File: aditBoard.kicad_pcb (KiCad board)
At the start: 4 copper layers, 36 parts, among them J1 USB_C_Receptacle_USB2.0, J2 Hashboard0, U2 W25X40CLUXIG TR, U3 RP2040, U4 RT9080-33GJ5, Y1 12MHz

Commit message: pretty much routed
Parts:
- removed R24, R26, R28: 4.7K, Resistor_SMD:R_0805_2012Metric
- added R1: 10k, Resistor_SMD:R_0402_1005Metric, F.Cu at (122.0, 97.8)
- J2: footprint Connector_PinHeader_2.00mm:PinHeader_2x09_P2.00mm_Horizontal -> aditBoard:PinHeader_2x09_P2.00mm_Horizontal
- R25, R27, R29: footprint Resistor_SMD:R_0805_2012Metric -> Resistor_SMD:R_0402_1005Metric
- TP1, TP4, TP5, TP6: moved to B.Cu
- moved C17 35.6 mm to (115.1, 99.2), turned to 90 degrees
- moved R4 35.0 mm to (115.1, 101.3), turned to -90 degrees
- moved J1 32.9 mm to (121.0, 107.1), turned to 0 degrees
- moved C18 32.9 mm to (116.9, 97.2)
- moved C11 32.7 mm to (115.0, 94.5), turned to 90 degrees
- moved C14 31.7 mm to (115.1, 84.2), turned to -90 degrees
- moved C13 30.7 mm to (116.0, 94.5), turned to 90 degrees
- moved R3 30.1 mm to (120.0, 98.9), turned to 90 degrees
- moved C9 29.6 mm to (115.1, 97.4), turned to -90 degrees
- moved R2 29.6 mm to (120.9, 98.9), turned to 90 degrees
- moved C8 29.4 mm to (115.5, 96.0)
- moved C16 29.3 mm to (123.6, 100.9), turned to 90 degrees
- moved C15 29.2 mm to (123.1, 97.8), turned to -90 degrees
- moved C10 27.9 mm to (116.2, 84.2), turned to -90 degrees
- moved C7 27.8 mm to (115.6, 81.6)
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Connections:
- net /A00 renamed /A0
- net /A10 renamed /A1
- net /A20 renamed /A2
- J2 pad 11: /TXD0 -> /TXD
- J2 pad 12: /RXD0 -> /RXD
- J2 pad 15: /RST0 -> /RST
- J2 pad 3: /SDA0 -> /SDA
- J2 pad 4: /SCL0 -> /SCL
- J2 pad 5: /PLUG0 -> /PLUG
- U3 pad 11: /UART_TX -> /TXD
- U3 pad 12: /UART_RX -> /RXD
- U3 pad 13: unconnected-(U3-GPIO10-Pad13) -> /PLUG
- U3 pad 14: unconnected-(U3-GPIO11-Pad14) -> /RST
- U3 pad 17: /I2C_SDA -> /SDA
- U3 pad 18: /I2C_SCL -> /SCL
- U3 pad 8: /POWERUP -> unconnected-(U3-GPIO6-Pad8)
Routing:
- net /GND: track 0.00 -> 27.3 mm, vias 0 -> 21
- net /1V1: track 0.00 -> 27.0 mm, vias 0 -> 7
- net /A2: track 0.00 -> 24.7 mm, vias 0 -> 1
- net /3V3: track 0.00 -> 19.2 mm, vias 0 -> 15
- net /A1: track 0.00 -> 17.9 mm, vias 0 -> 1
- net /5V: track 0.00 -> 13.4 mm, vias 0 -> 2
- net /A0: track 0.00 -> 13.0 mm, vias 0 -> 1
- net /RST: track 0.00 -> 10.7 mm, vias 0 -> 1
- net /SCL: track 0.00 -> 8.73 mm, vias 0 -> 1
- net Net-(J1-CC1): track 0.00 -> 8.42 mm
- net /QSPI_SS: track 0.00 -> 8.36 mm, vias 0 -> 1
- net Net-(U3-USB_DP): track 0.00 -> 8.00 mm
- net Net-(J1-CC2): track 0.00 -> 7.98 mm
- net Net-(U3-USB_DM): track 0.00 -> 7.33 mm
- net /RXD: track 0.00 -> 7.08 mm
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- added copper zone on In2.Cu, net /3V3
- added copper zone on In1.Cu, net /GND
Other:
- board outline added: 13.2 x 30 mm

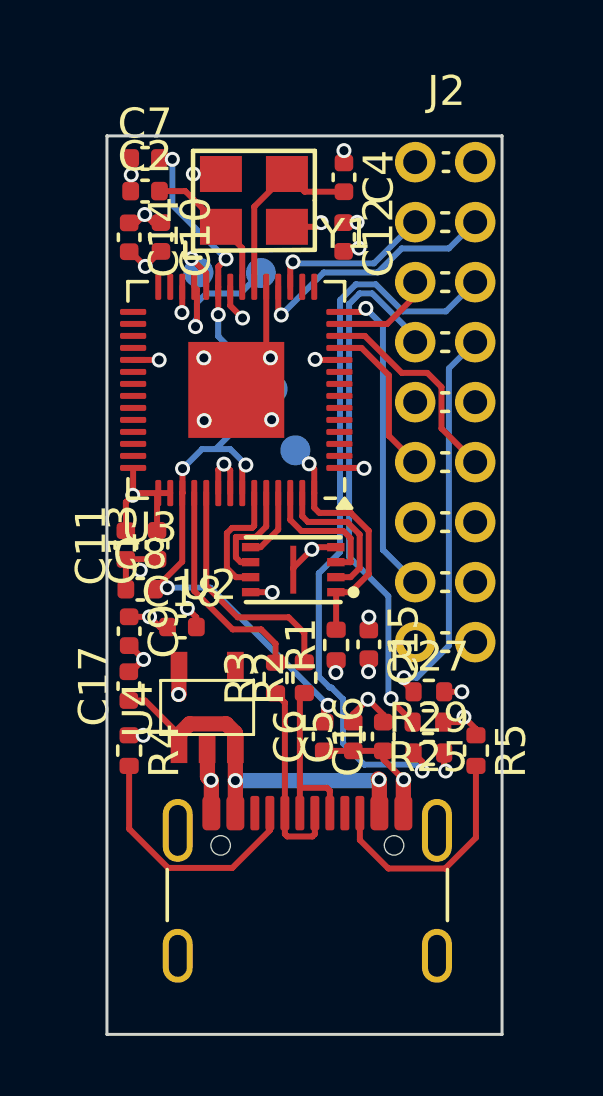
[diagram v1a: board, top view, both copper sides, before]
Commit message: added artwork, DRC, LCSC BOM
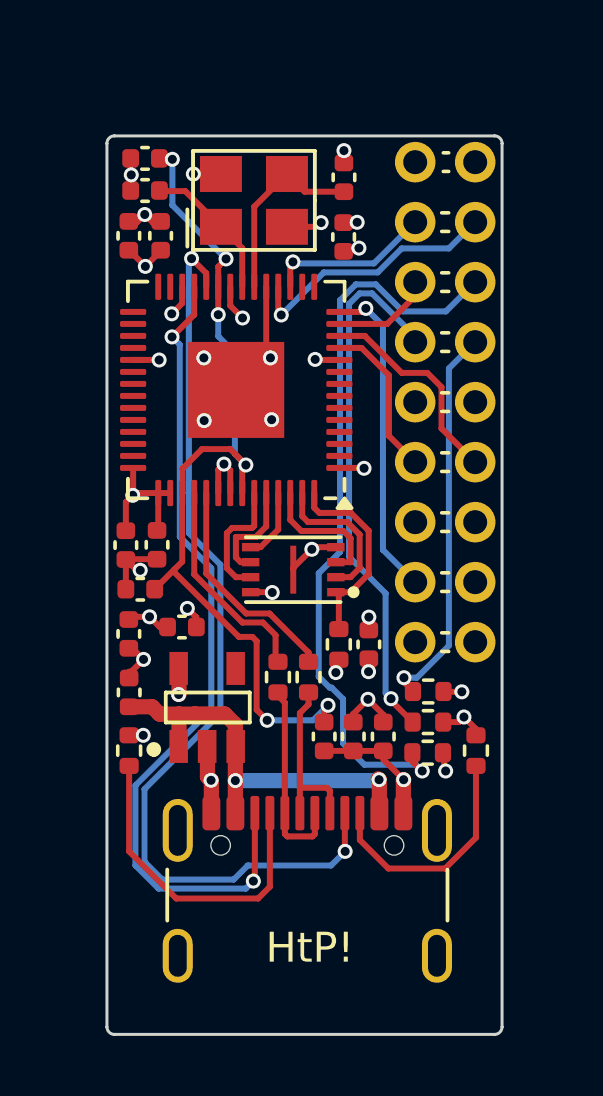
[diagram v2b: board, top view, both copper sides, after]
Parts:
- removed TP1, TP4, TP5, TP6: TestPoint, TestPoint:TestPoint_Pad_D1.0mm
- added G***: LOGO, aditBoard:logo, B.Cu at (119.8, 95.7)
- U4: value RT9080-33GJ5 -> AP2112K-3.3TRG1; footprint aditBoard:RT9080-33GJ5 -> aditBoard:SOT-25-5_L2.9-W1.6-P0.95-LS2.8-BL
- moved C17 0.21 mm to (115.1, 99.4)
- moved R2 0.14 mm to (121.1, 98.9)
- moved R1 0.09 mm to (122.1, 97.8)
- moved C9 0.09 mm to (115.1, 97.5)
- moved R3 0.09 mm to (120.1, 98.9)
- moved C14 0.05 mm to (115.1, 84.2)
- turned U4 to 0 degrees
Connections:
- J1 pad A8: unconnected-(J1-SBU1-PadA8) -> /SWCLK
- J1 pad B8: unconnected-(J1-SBU2-PadB8) -> /SWD
- U3 pad 24: Net-(U3-SWCLK) -> /SWCLK
- U3 pad 25: Net-(U3-SWD) -> /SWD
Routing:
- net /SWCLK: track 0.00 -> 31.4 mm, vias 0 -> 2
- net /SWD: track 0.00 -> 27.8 mm, vias 0 -> 2
- net Net-(U3-SWD): track 4.74 -> 0.00 mm, vias 1 -> 0
- net Net-(J1-CC1): track 8.42 -> 10.8 mm
- net /1V1: track 27.0 -> 29.3 mm, vias 7 -> 6
- net /QSPI_SS: track 8.36 -> 6.68 mm, vias 1 -> 0
- net Net-(U3-SWCLK): track 1.14 -> 0.00 mm, vias 1 -> 0
- net /GND: track 27.3 -> 26.3 mm
- net Net-(U3-USB_DP): track 8.00 -> 7.49 mm
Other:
- outline, holes or cut-outs redrawn
- board text added: "HtP!"
- board text added: "v1"

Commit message: add readme
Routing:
- net /A2: track 24.7 -> 23.4 mm
- net Net-(J1-CC2): track 7.98 -> 8.90 mm
- net /RXD: track 7.08 -> 7.66 mm
